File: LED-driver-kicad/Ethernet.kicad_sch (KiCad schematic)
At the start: 23 parts, among them J1 ARJM11C7-114-BA-EW2, U8 ENC28J60x-SO, Y1 25MHz

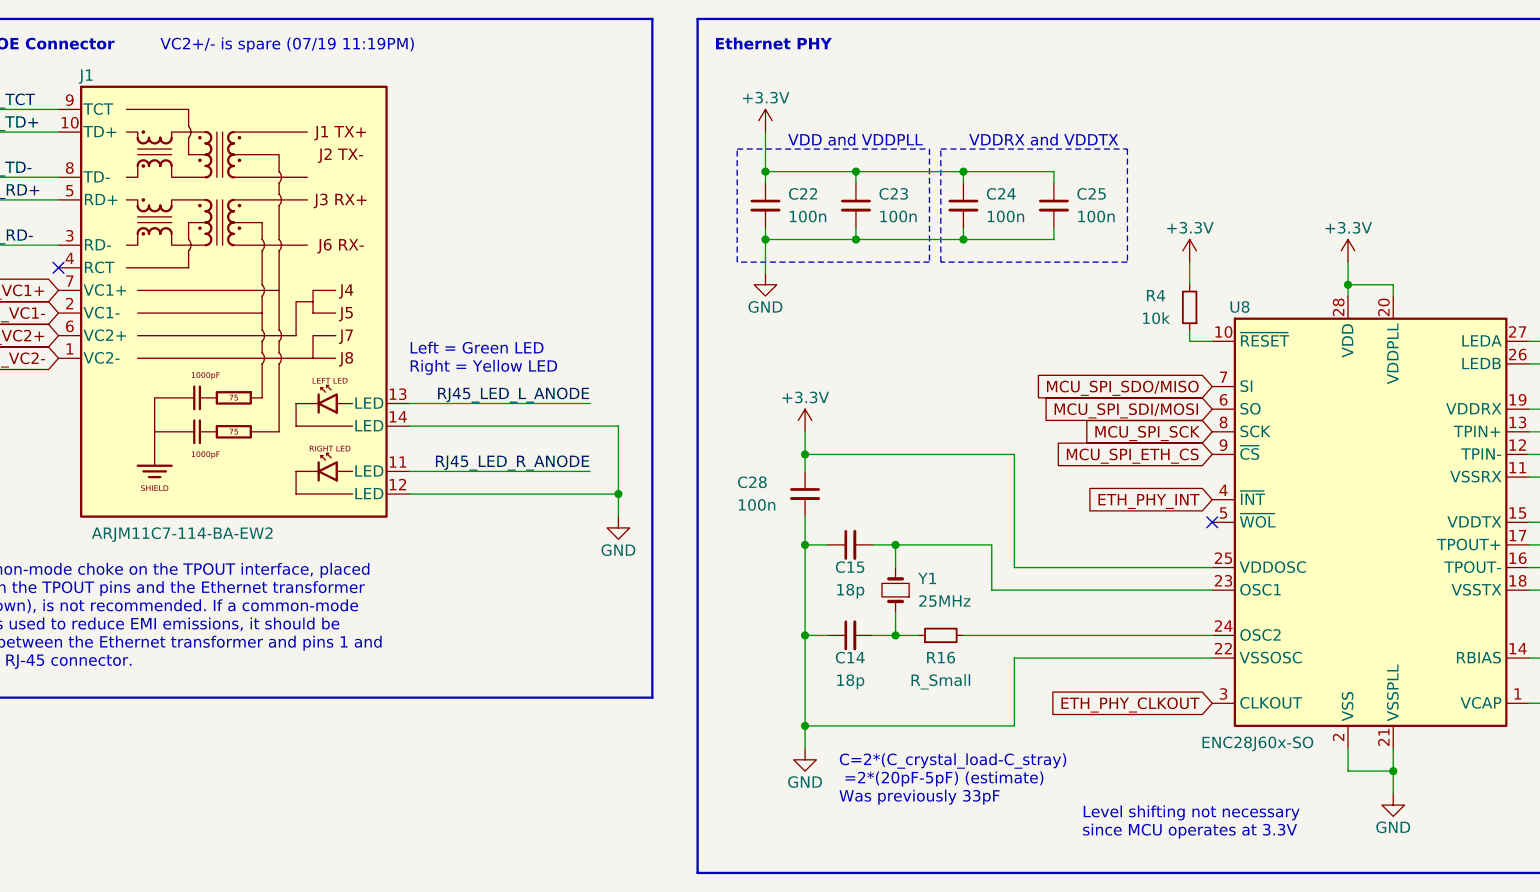
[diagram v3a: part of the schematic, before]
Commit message: update comments and title blocks
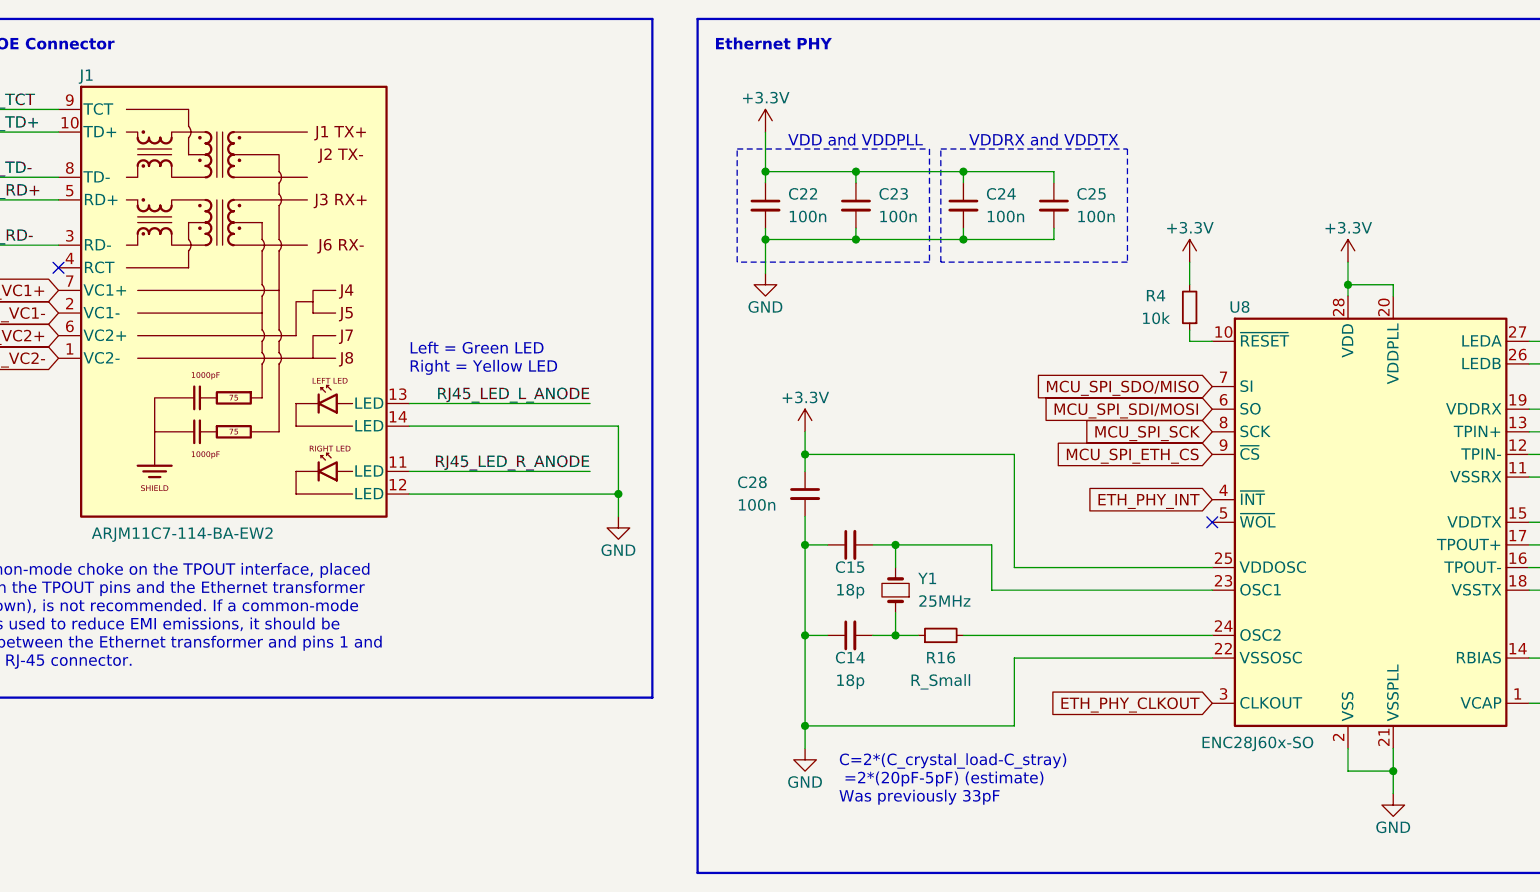
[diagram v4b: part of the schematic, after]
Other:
- note removed: "Level shifting not necessary since MCU operates at 3.3V"
- note removed: "VC2+/- is spare (07/19 11:19PM)"
- title: (none) -> Photogrammetry Rig - LED Driver
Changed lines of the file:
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@@
 (kicad_sch (version 20230121) (generator eeschema)
   (paper "A4")
+  (title_block
+    (title "Photogrammetry Rig - LED Driver")
+    (date "2023-08-02")
+    (rev "0.1.0")
+  )
   (junction (at 222.25 92.075) (diameter 0) (color 0 0 0 0)
   )
@@
     (effects (font (size 1.27 1.27) (thickness 0.254) bold) (justify left bottom))
   )
-  (text "Level shifting not necessary\nsince MCU operates at 3.3V"
-    (at 146.685 107.315 0)
-    (effects (font (size 1.27 1.27)) (justify left bottom))
-  )
   (text "Ethernet PHY" (at 105.41 19.05 0)
     (effects (font (size 1.27 1.27) (thickness 0.254) bold) (justify left bottom))
   )
-  (text "VC2+/- is spare (07/19 11:19PM)\n" (at 43.18 19.05 0)
-    (effects (font (size 1.27 1.27)) (justify left bottom))
-  )
   (text "VDD and VDDPLL" (at 113.665 29.845 0)

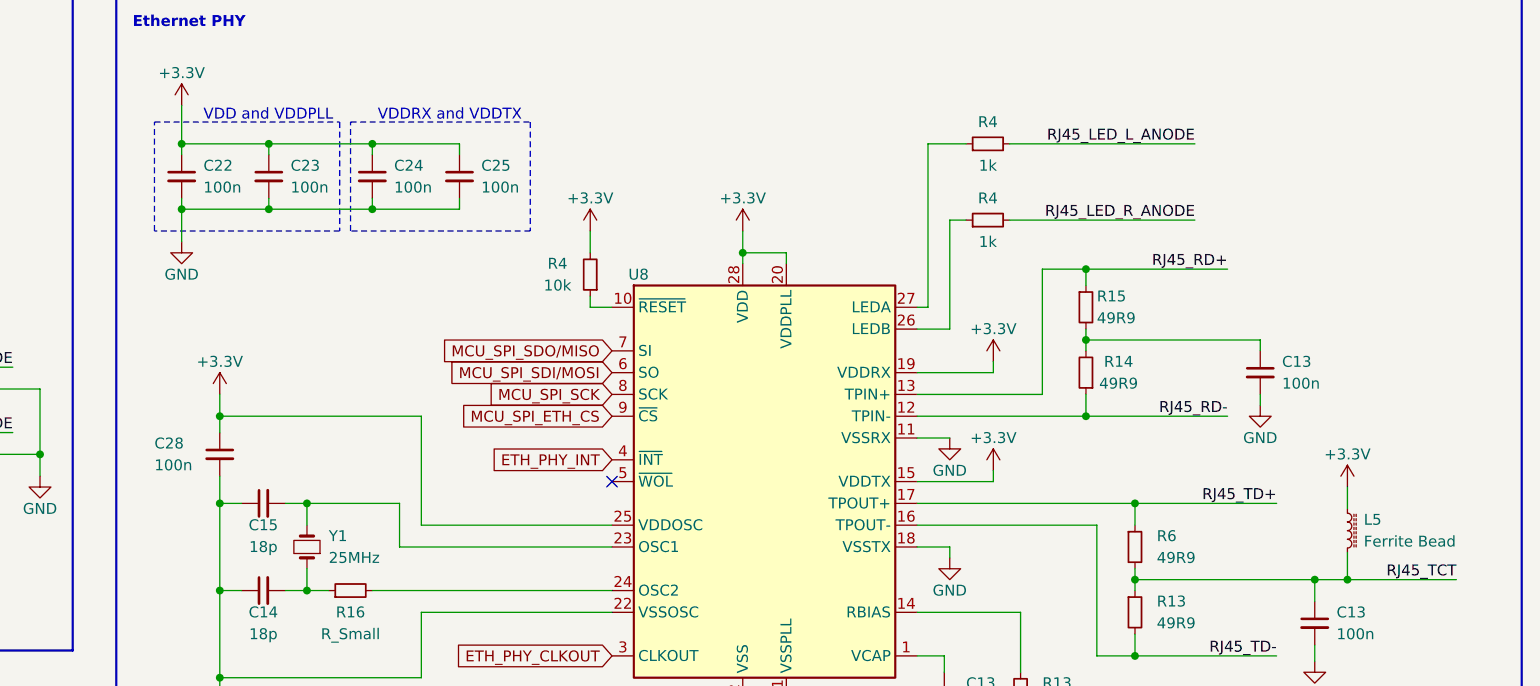
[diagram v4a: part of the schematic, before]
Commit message: update component designators
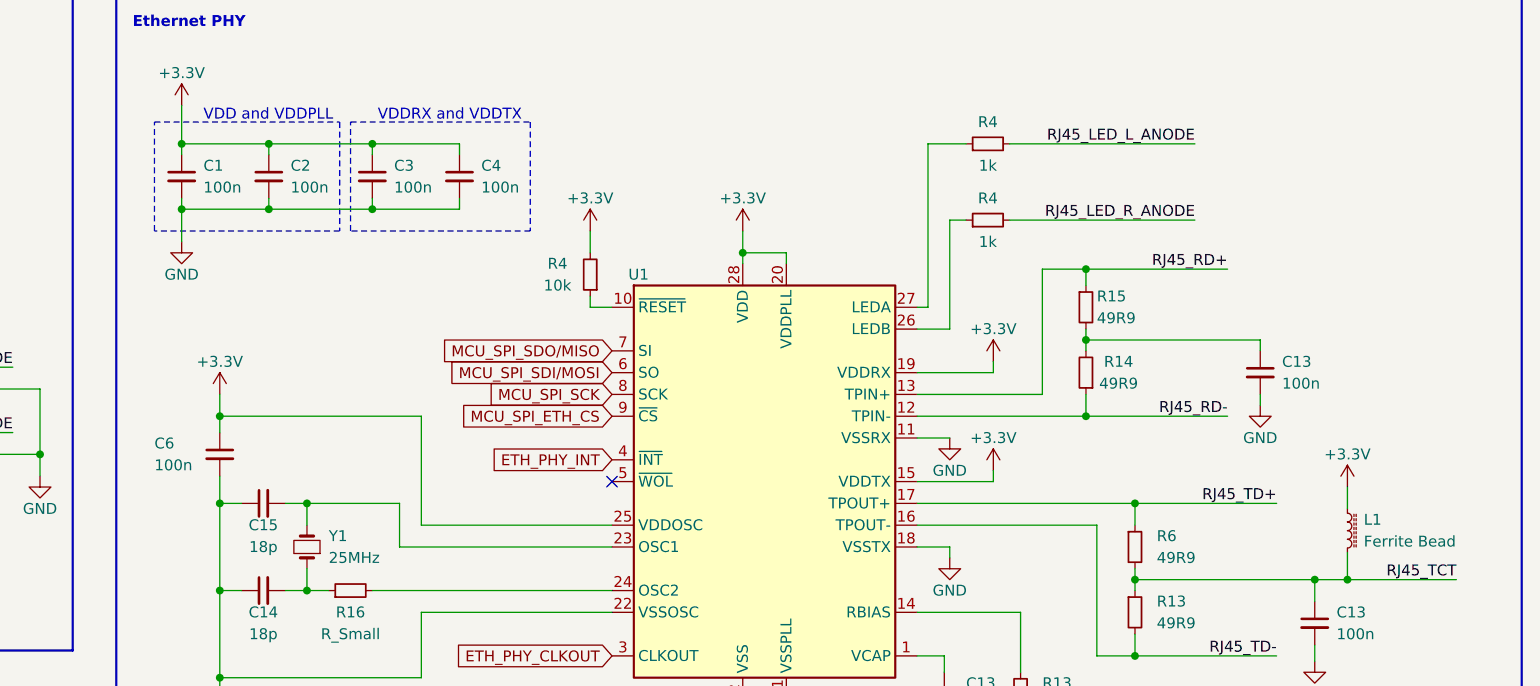
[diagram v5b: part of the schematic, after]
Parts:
- renumbered C22 to C1, C23 to C2, C24 to C3, C25 to C4, C28 to C6, L5 to L1, U8 to U1

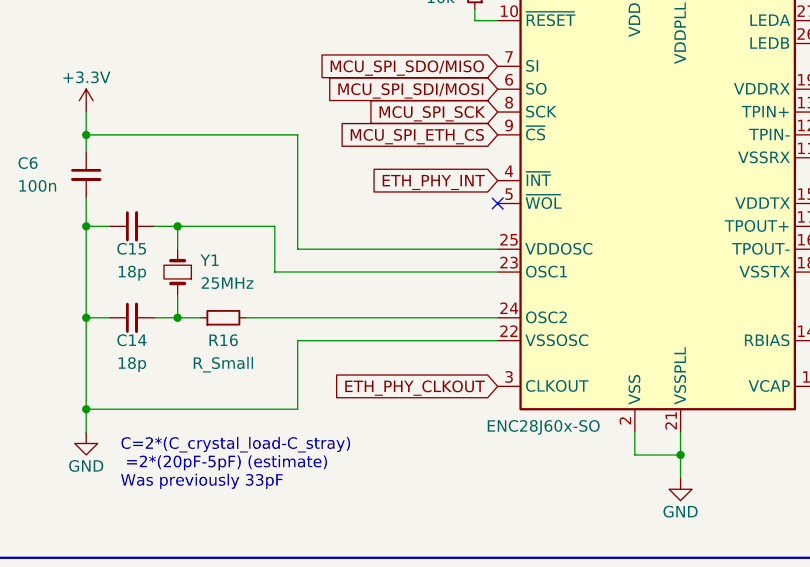
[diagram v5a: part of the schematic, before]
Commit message: resolve Electrical Rules Checker (ERC) errors and warnings
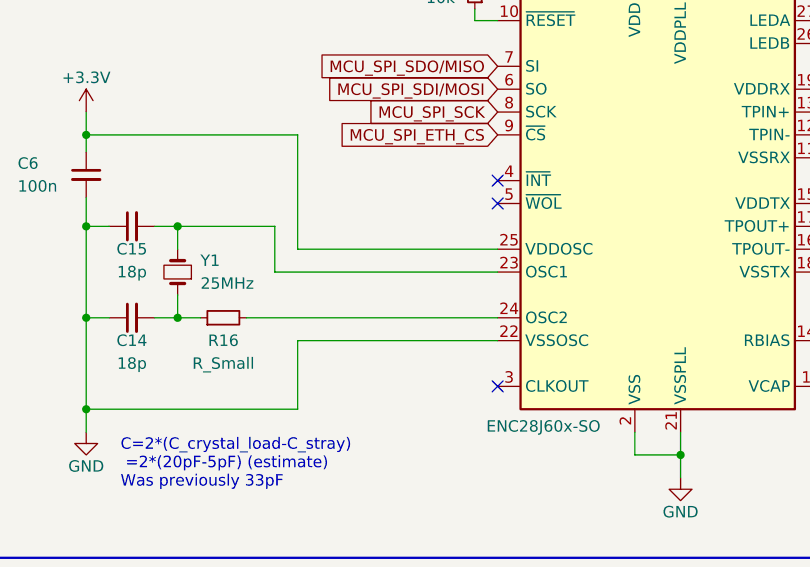
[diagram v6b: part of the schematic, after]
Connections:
- net ETH_PHY_CLKOUT: no longer names the net of U1.3 (CLKOUT)
- net ETH_PHY_INT: no longer names the net of U1.4 (~{INT})
- no-connect marks 2 -> 4
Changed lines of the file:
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@@
   )
   (no_connect (at 31.75 43.18))
+  (no_connect (at 161.29 69.215))
+  (no_connect (at 161.29 92.075))
   (no_connect (at 161.29 71.755))
   (wire (pts (xy 125.73 74.295) (xy 136.525 74.295))
@@
     )
   )
-  (global_label "ETH_PHY_CLKOUT" (shape input) (at 161.29 92.075 180) (fields_autoplaced)
-    (effects (font (size 1.27 1.27)) (justify right))
-    (property "Intersheetrefs" "${INTERSHEET_REFS}" (at 142.0367 92.075 0)
-      (effects (font (size 1.27 1.27)) (justify right) hide)
-    )
-  )
   (global_label "MCU_SPI_SDI{slash}MOSI" (shape input) (at 161.29 59.055 180) (fields_autoplaced)
     (effects (font (size 1.27 1.27)) (justify right))
@@
     (effects (font (size 1.27 1.27)) (justify right))
     (property "Intersheetrefs" "${INTERSHEET_REFS}" (at 145.4839 61.595 0)
-      (effects (font (size 1.27 1.27)) (justify right) hide)
-    )
-  )
-  (global_label "ETH_PHY_INT" (shape input) (at 161.29 69.215 180) (fields_autoplaced)
-    (effects (font (size 1.27 1.27)) (justify right))
-    (property "Intersheetrefs" "${INTERSHEET_REFS}" (at 146.3305 69.215 0)
       (effects (font (size 1.27 1.27)) (justify right) hide)
     )
@@
     )
   )
-  (symbol (lib_id "power:GND") (at 200.66 80.645 0) (unit 1)
-    (in_bom yes) (on_board yes) (dnp no)
-    (property "Reference" "#PWR021" (at 200.66 86.995 0)
-      (effects (font (size 1.27 1.27)) hide)
-    )
-    (property "Value" "GND" (at 200.66 84.455 0)
-      (effects (font (size 1.27 1.27)))
-    )
-    (property "Footprint" "" (at 200.66 80.645 0)
-      (effects (font (size 1.27 1.27)) hide)
-    )
-    (property "Datasheet" "" (at 200.66 80.645 0)
-      (effects (font (size 1.27 1.27)) hide)
-    )
-    (pin "1")
-    (instances
-      (project "LED-driver-kicad"
-        (path "/2b071084-2ab6-4896-84cc-45b211479417"
-          (reference "#PWR021") (unit 1)
-        )
-        (path "/2b071084-2ab6-4896-84cc-45b211479417/359e4c60-3d39-46c5-bd25-b25d83369b39"
-          (reference "#PWR012") (unit 1)
-        )
-      )
-    )
-  )
   (symbol (lib_id "Device:R_Small") (at 222.25 79.375 0) (unit 1)
     (in_bom yes) (on_board yes) (dnp no) (fields_autoplaced)
@@
         (path "/2b071084-2ab6-4896-84cc-45b211479417/359e4c60-3d39-46c5-bd25-b25d83369b39"
           (reference "R6") (unit 1)
+        )
+      )
+    )
+  )
+  (symbol (lib_id "power:GND") (at 200.66 66.675 0) (unit 1)
+    (in_bom yes) (on_board yes) (dnp no)
+    (property "Reference" "#PWR09" (at 200.66 73.025 0)
+      (effects (font (size 1.27 1.27)) hide)
+    )
+    (property "Value" "GND" (at 200.66 70.485 0)
+      (effects (font (size 1.27 1.27)))
+    )
+    (property "Footprint" "" (at 200.66 66.675 0)
+      (effects (font (size 1.27 1.27)) hide)
+    )
+    (property "Datasheet" "" (at 200.66 66.675 0)
+      (effects (font (size 1.27 1.27)) hide)
+    )
+    (pin "1")
+    (instances
+      (project "LED-driver-kicad"
+        (path "/2b071084-2ab6-4896-84cc-45b211479417/359e4c60-3d39-46c5-bd25-b25d83369b39"
+          (reference "#PWR09") (unit 1)
         )
       )
@@
     )
   )
-  (symbol (lib_id "power:GND") (at 200.66 66.675 0) (unit 1)
-    (in_bom yes) (on_board yes) (dnp no)
-    (property "Reference" "#PWR021" (at 200.66 73.025 0)
-      (effects (font (size 1.27 1.27)) hide)
-    )
-    (property "Value" "GND" (at 200.66 70.485 0)
-      (effects (font (size 1.27 1.27)))
-    )
-    (property "Footprint" "" (at 200.66 66.675 0)
-      (effects (font (size 1.27 1.27)) hide)
-    )
-    (property "Datasheet" "" (at 200.66 66.675 0)
-      (effects (font (size 1.27 1.27)) hide)
-    )
-    (pin "1")
-    (instances
-      (project "LED-driver-kicad"
-        (path "/2b071084-2ab6-4896-84cc-45b211479417"
-          (reference "#PWR021") (unit 1)
-        )
-        (path "/2b071084-2ab6-4896-84cc-45b211479417/359e4c60-3d39-46c5-bd25-b25d83369b39"
-          (reference "#PWR08") (unit 1)
-        )
-      )
-    )
-  )
   (symbol (lib_id "Device:R_Small") (at 130.81 84.455 90) (unit 1)
     (in_bom yes) (on_board yes) (dnp no)
@@
     )
   )
-  (symbol (lib_id "power:+3.3V") (at 205.74 70.485 0) (unit 1)
-    (in_bom yes) (on_board yes) (dnp no)
-    (property "Reference" "#PWR09" (at 205.74 74.295 0)
-      (effects (font (size 1.27 1.27)) hide)
-    )
-    (property "Value" "+3.3V" (at 205.74 66.675 0)
-      (effects (font (size 1.27 1.27)))
-    )
-    (property "Footprint" "" (at 205.74 70.485 0)
-      (effects (font (size 1.27 1.27)) hide)
-    )
-    (property "Datasheet" "" (at 205.74 70.485 0)
-      (effects (font (size 1.27 1.27)) hide)
-    )
-    (pin "1")
-    (instances
-      (project "LED-driver-kicad"
-        (path "/2b071084-2ab6-4896-84cc-45b211479417/359e4c60-3d39-46c5-bd25-b25d83369b39"
-          (reference "#PWR09") (unit 1)
-        )
-      )
-    )
-  )
   (symbol (lib_id "power:GND") (at 94.615 71.12 0) (unit 1)
     (in_bom yes) (on_board yes) (dnp no)
@@
         (path "/2b071084-2ab6-4896-84cc-45b211479417/359e4c60-3d39-46c5-bd25-b25d83369b39"
           (reference "#PWR010") (unit 1)
+        )
+      )
+    )
+  )
+  (symbol (lib_id "power:GND") (at 200.66 80.645 0) (unit 1)
+    (in_bom yes) (on_board yes) (dnp no)
+    (property "Reference" "#PWR08" (at 200.66 86.995 0)
+      (effects (font (size 1.27 1.27)) hide)
+    )
+    (property "Value" "GND" (at 200.66 84.455 0)
+      (effects (font (size 1.27 1.27)))
+    )
+    (property "Footprint" "" (at 200.66 80.645 0)
+      (effects (font (size 1.27 1.27)) hide)
+    )
+    (property "Datasheet" "" (at 200.66 80.645 0)
+      (effects (font (size 1.27 1.27)) hide)
+    )
+    (pin "1")
+    (instances
+      (project "LED-driver-kicad"
+        (path "/2b071084-2ab6-4896-84cc-45b211479417/359e4c60-3d39-46c5-bd25-b25d83369b39"
+          (reference "#PWR08") (unit 1)
         )
       )
@@
         )
       )
+    )
+  )
+  (symbol (lib_id "power:+3.3V") (at 205.74 70.485 0) (unit 1)
+    (in_bom yes) (on_board yes) (dnp no)
+    (property "Reference" "#PWR054" (at 205.74 74.295 0)
+      (effects (font (size 1.27 1.27)) hide)
+    )
+    (property "Value" "+3.3V" (at 205.74 66.675 0)
+      (effects (font (size 1.27 1.27)))
+    )
+    (property "Footprint" "" (at 205.74 70.485 0)
+      (effects (font (size 1.27 1.27)) hide)
+    )
+    (property "Datasheet" "" (at 205.74 70.485 0)
+      (effects (font (size 1.27 1.27)) hide)
+    )
+    (pin "1")
+    (instances
+      (project "LED-driver-kicad"
+        (path "/2b071084-2ab6-4896-84cc-45b211479417/359e4c60-3d39-46c5-bd25-b25d83369b39"
+          (reference "#PWR054") (unit 1)
+        )
+      )
